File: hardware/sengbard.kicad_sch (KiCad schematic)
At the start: 0 parts

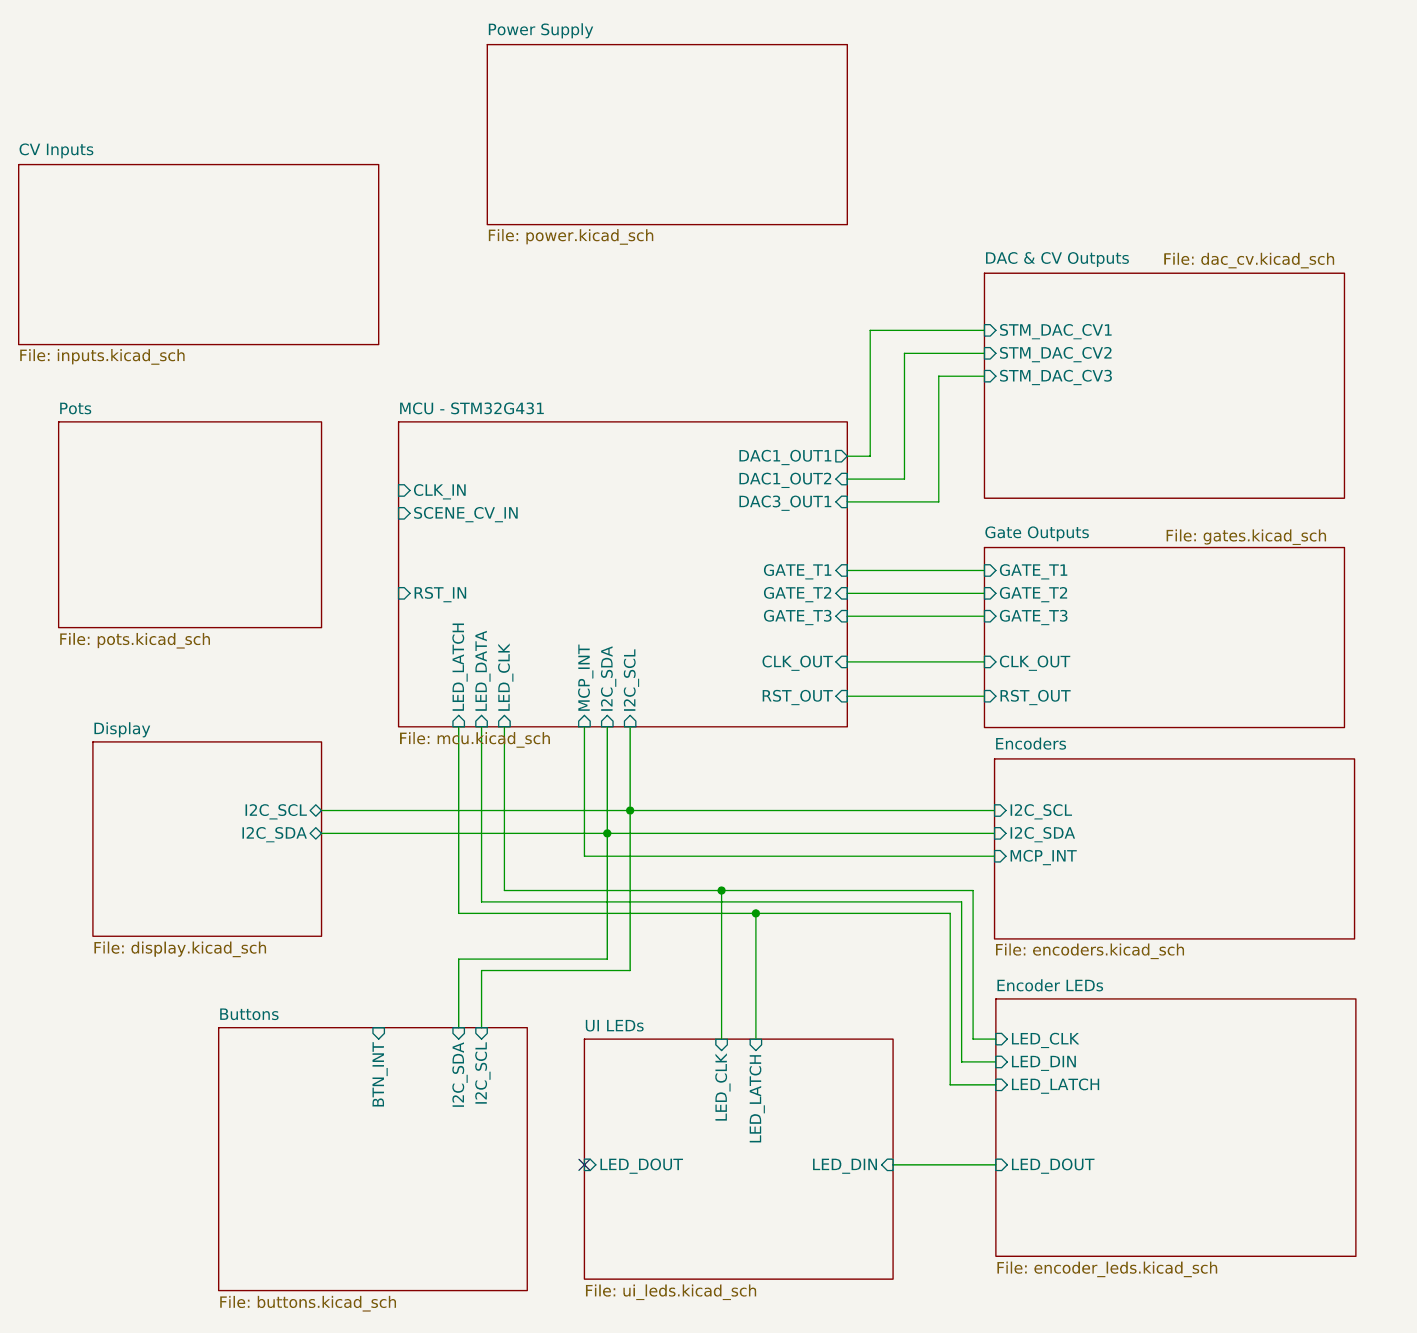
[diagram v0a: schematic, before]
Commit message: Complete hierarchical schematic sheets and fix wiring
- Complete encoder_leds sheet with MAX7219 + 64 LEDs
- Complete ui_leds sheet with MAX7219 + 45 LEDs
- Complete buttons sheet with MCP23017 + 40 buttons
- Complete display sheet with OLED I2C connector
- Complete pots sheet with 3 potentiometers
- Complete encoders sheet with 8 rotary encoders on MCP23017
- Fix inputs sheet hierarchical labels (CLK_IN, RST_IN, SCENE_CV_IN)
- Update MCU sheet with ADC hierarchical labels
- Update root sheet with hierarchical pin connections
- Various ERC fixes and wiring corrections

Co-Authored-By: Claude Opus 4.5 <noreply@anthropic.com>
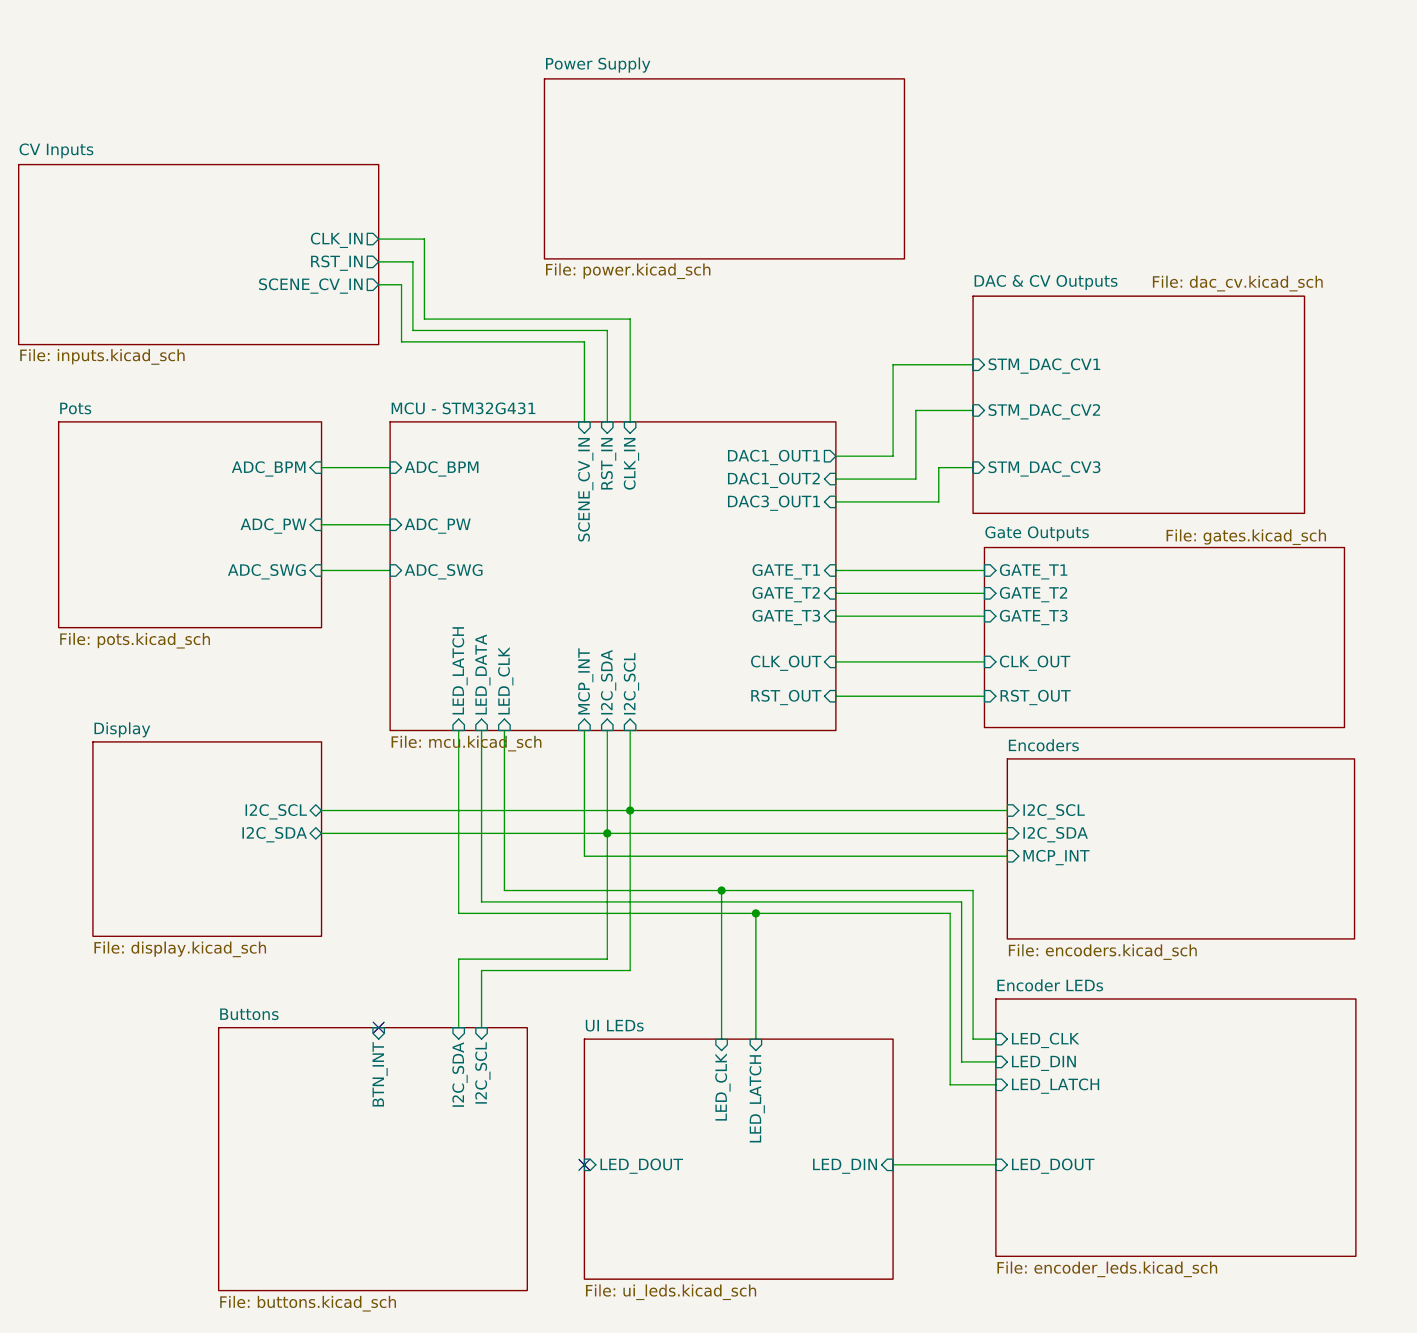
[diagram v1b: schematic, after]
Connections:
- no-connect marks 1 -> 2
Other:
- sheet CV Inputs ports: added CLK_IN, RST_IN, SCENE_CV_IN; removed none
- sheet MCU - STM32G431 ports: added ADC_BPM, ADC_PW, ADC_SWG; removed none
- sheet Pots ports: added ADC_BPM, ADC_PW, ADC_SWG; removed none
